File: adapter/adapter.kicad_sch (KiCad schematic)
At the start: 22 parts, among them J10 Ribbon, J11 Ribbon, J12 Ribbon, J13 serial, J14 serial, J3 battery charge, J6 battery charge, J7 trackball, J8 trackball, J9 Ribbon, SW1 SW_SPST, SW2 SW_SPST, SW3 SW_SPDT, SW4 SW_SPDT, U1 eliteC, U2 eliteC

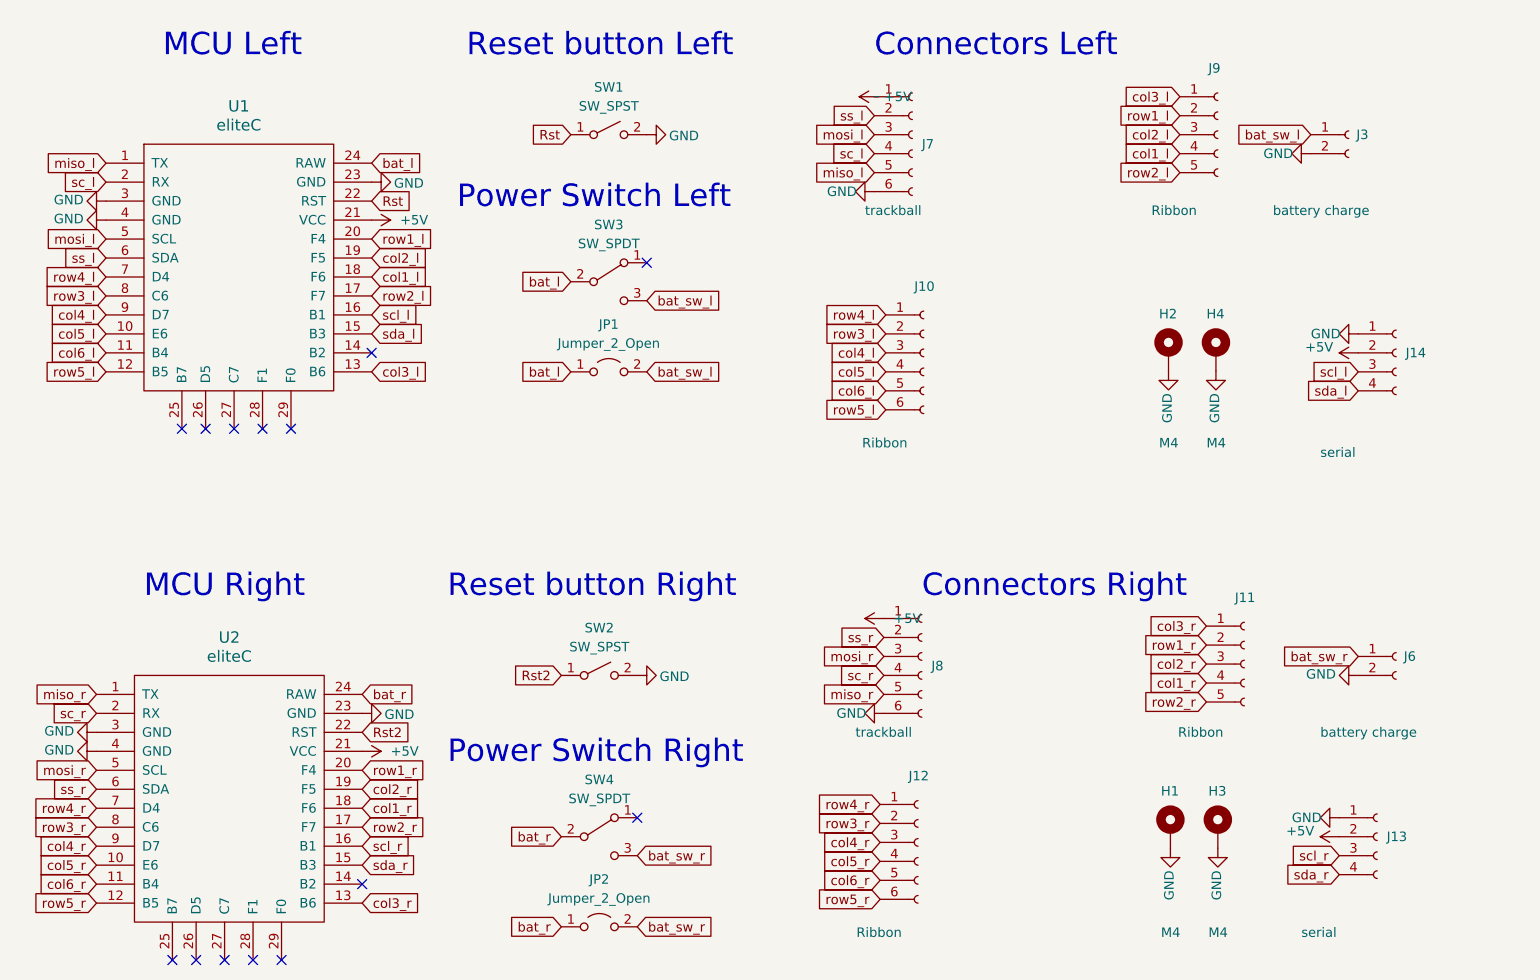
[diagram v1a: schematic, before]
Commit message: Remove serial from schematic
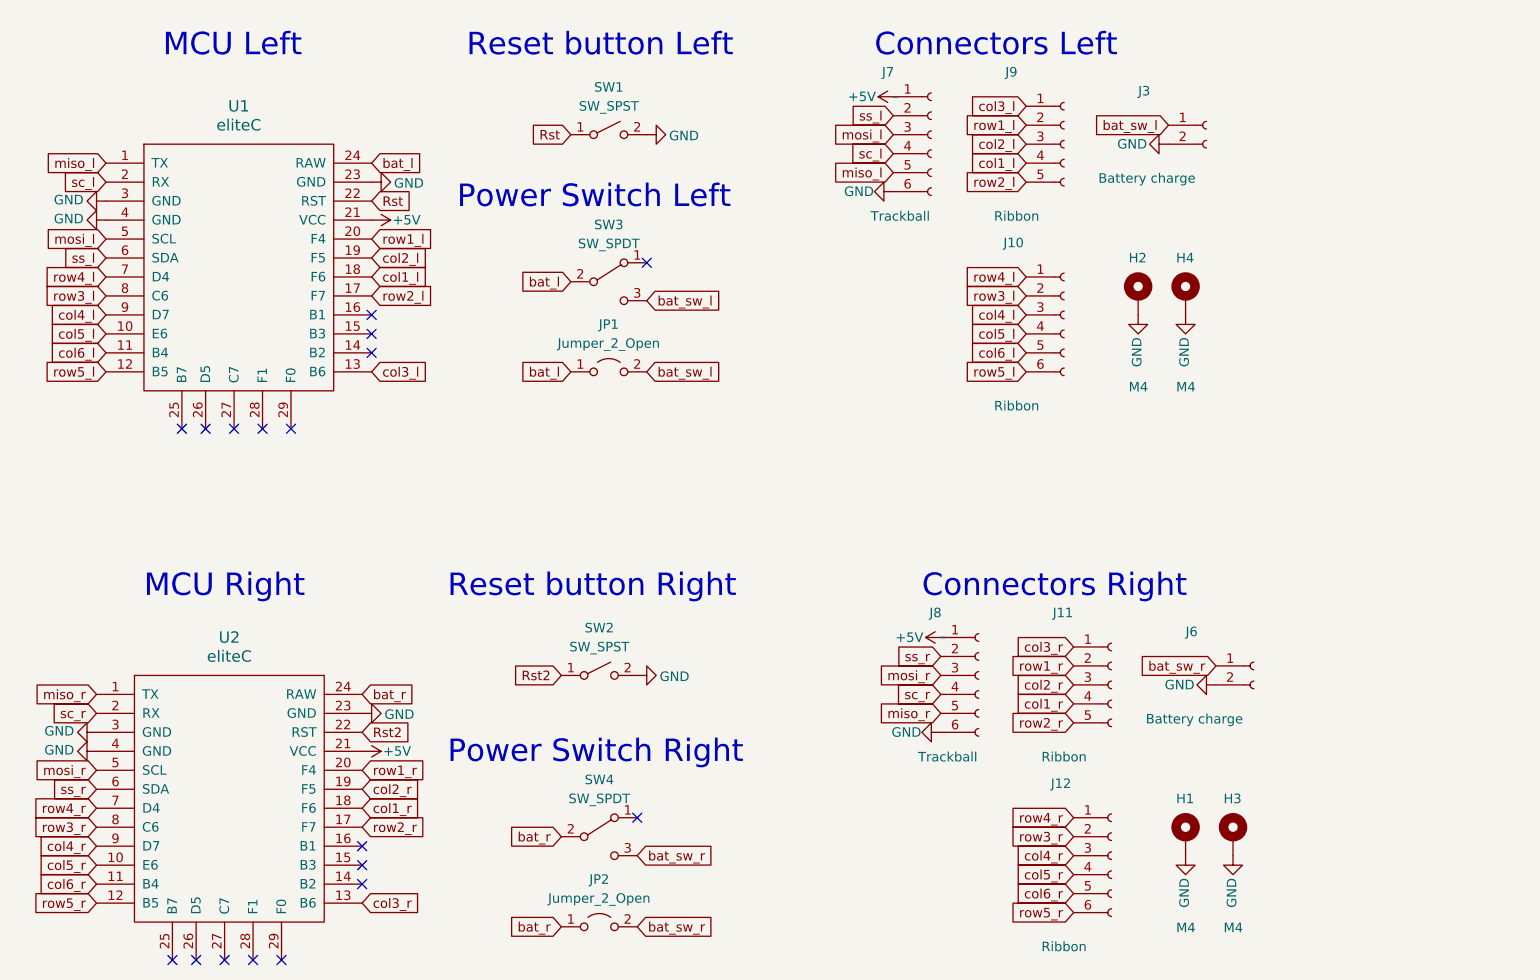
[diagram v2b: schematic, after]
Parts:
- removed J13, J14: serial, Library:PinHeader_1x04_P2.54mm_Vertical, symbol Connector:Conn_01x04_Female
- J3, J6: value battery charge -> Battery charge
- J7, J8: value trackball -> Trackball
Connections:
- net scl_l: no longer names the net of U1.16 (B1)
- net scl_r: no longer names the net of U2.16 (B1)
- net sda_l: no longer names the net of U1.15 (B3)
- net sda_r: no longer names the net of U2.15 (B3)
- no-connect marks 14 -> 18
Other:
- moved on the sheet: H2, H4, J10, J3, J7, J9

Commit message: Move reset button and power switch
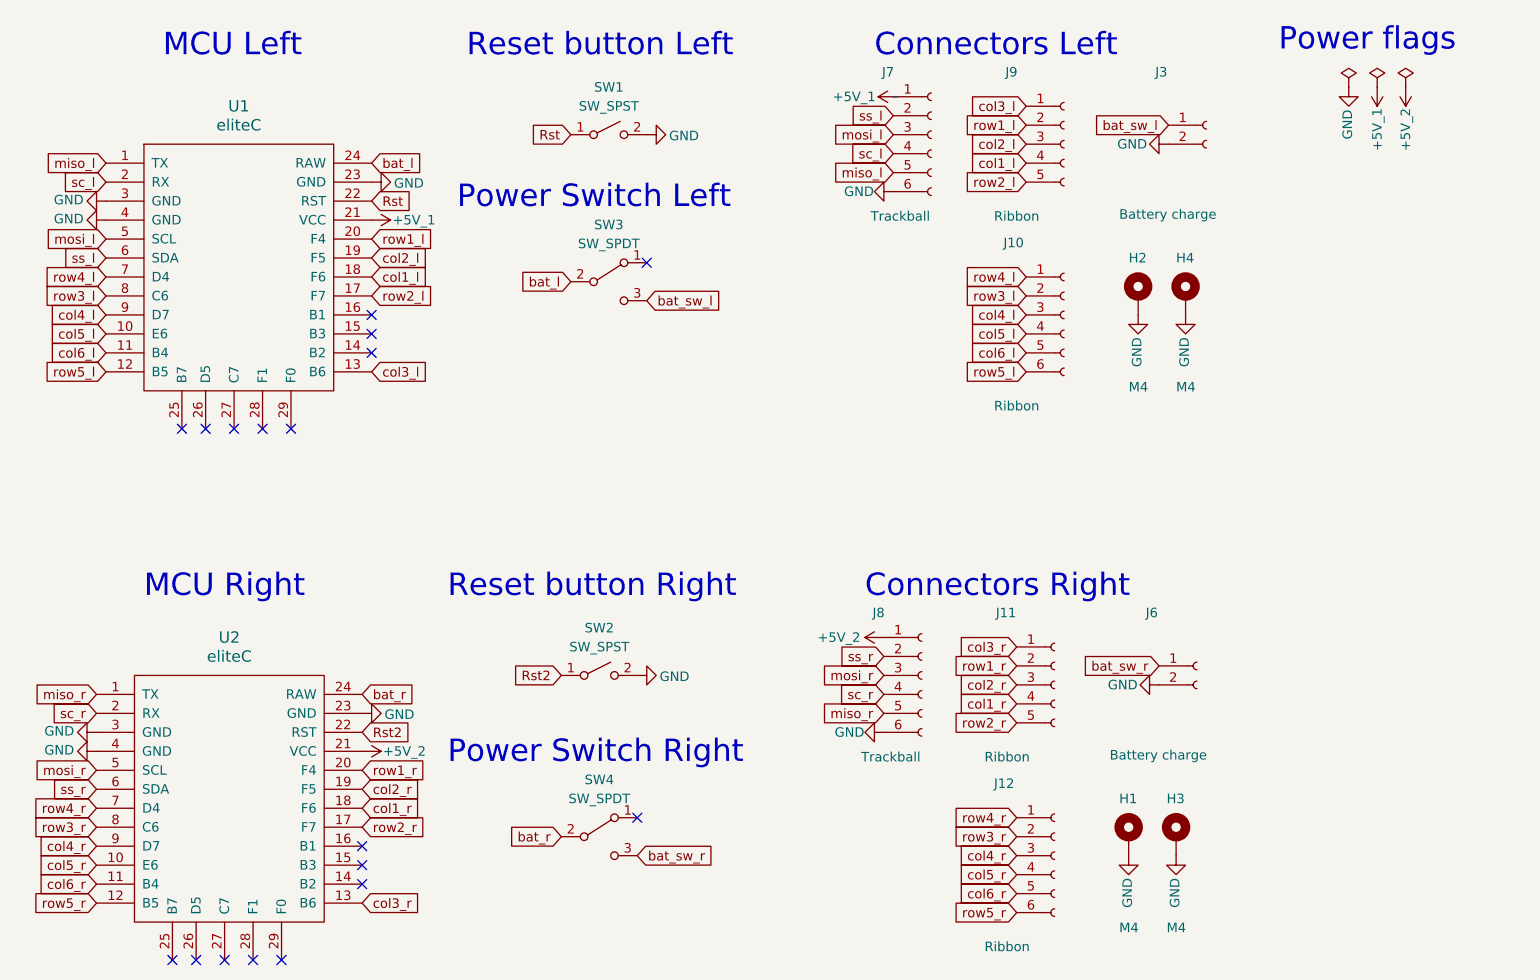
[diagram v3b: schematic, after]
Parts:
- removed JP1, JP2: Jumper_2_Open, Library:power_switch_jumper, symbol Jumper:Jumper_2_Open
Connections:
- net +5V renamed +5V_1
- net +5V_1: no longer J8.1 (Pin_1), U2.21 (VCC)
- new net +5V_2: J8.1 (Pin_1), U2.21 (VCC)
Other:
- note added: "Power flags"
- moved on the sheet: H1, H3, J11, J12, J8
